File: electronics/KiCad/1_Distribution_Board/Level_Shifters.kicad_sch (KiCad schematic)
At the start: 26 parts, among them J25 Generic 2.54mm, J26 Generic 2.54mm, J27 Generic 2.54mm, J28 Generic 2.54mm, J29 Generic 2.54mm, J30 Generic 2.54mm, J31 Conn_01x04, J32 Conn_01x04, Q2 TBD, Q3 TBD

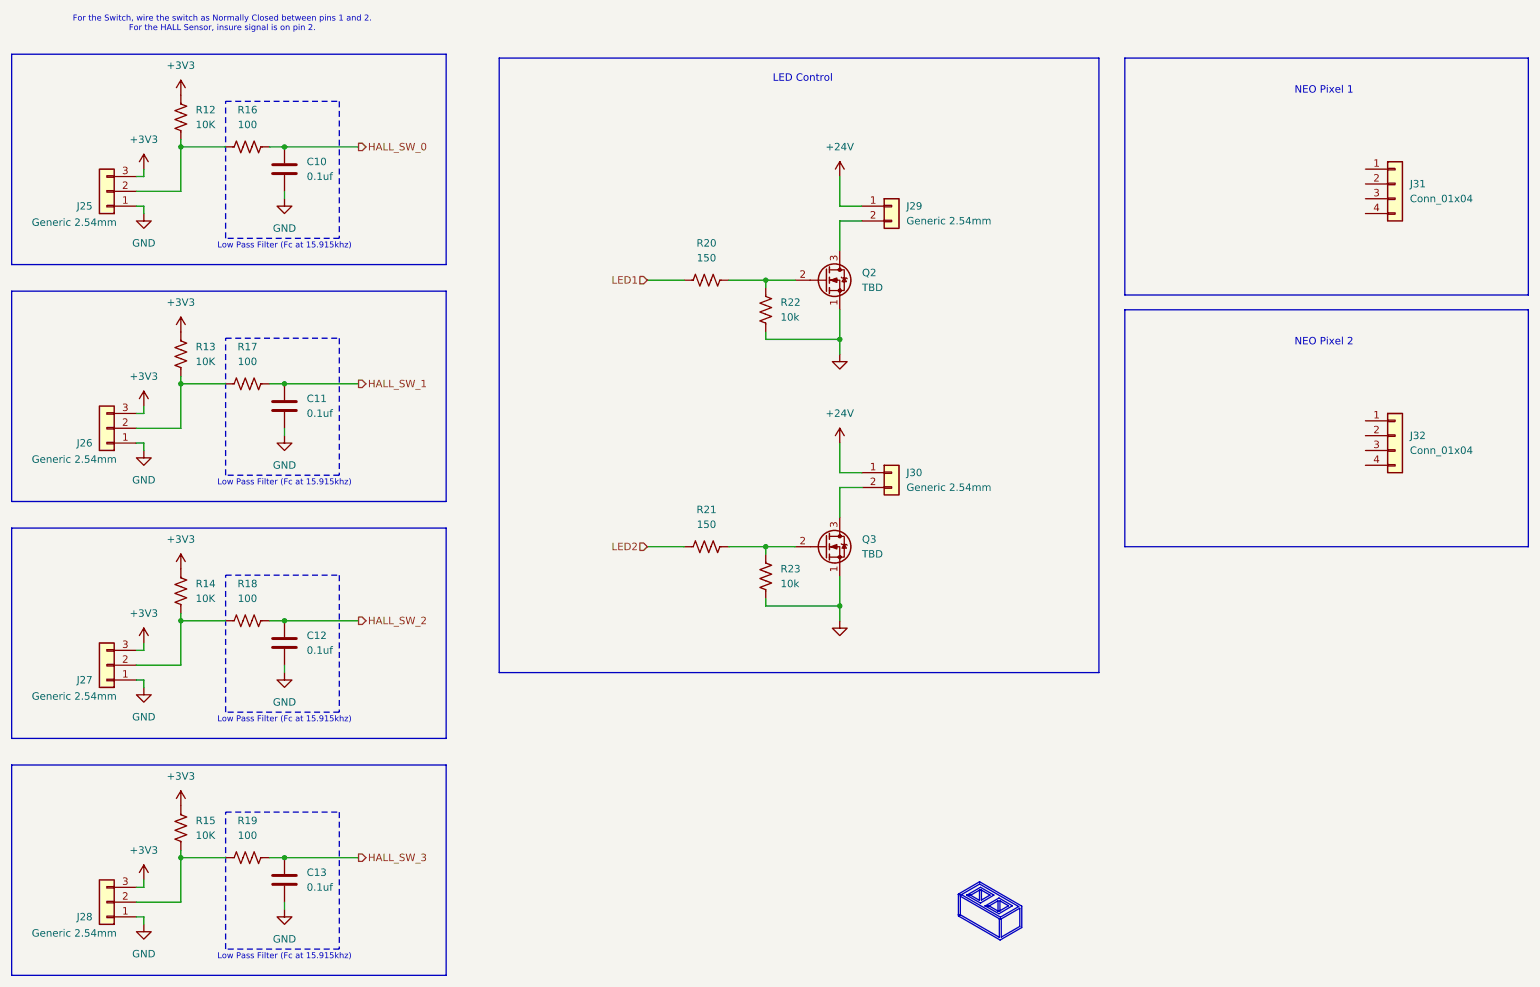
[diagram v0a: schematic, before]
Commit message: Additional Routing and placement
Updated power page on schematic to remove redundant connections. Removed test points on steppers since the steppers drivers chosen have test points on them. Updated placement and cleaned up silk. Started placing final power connections.
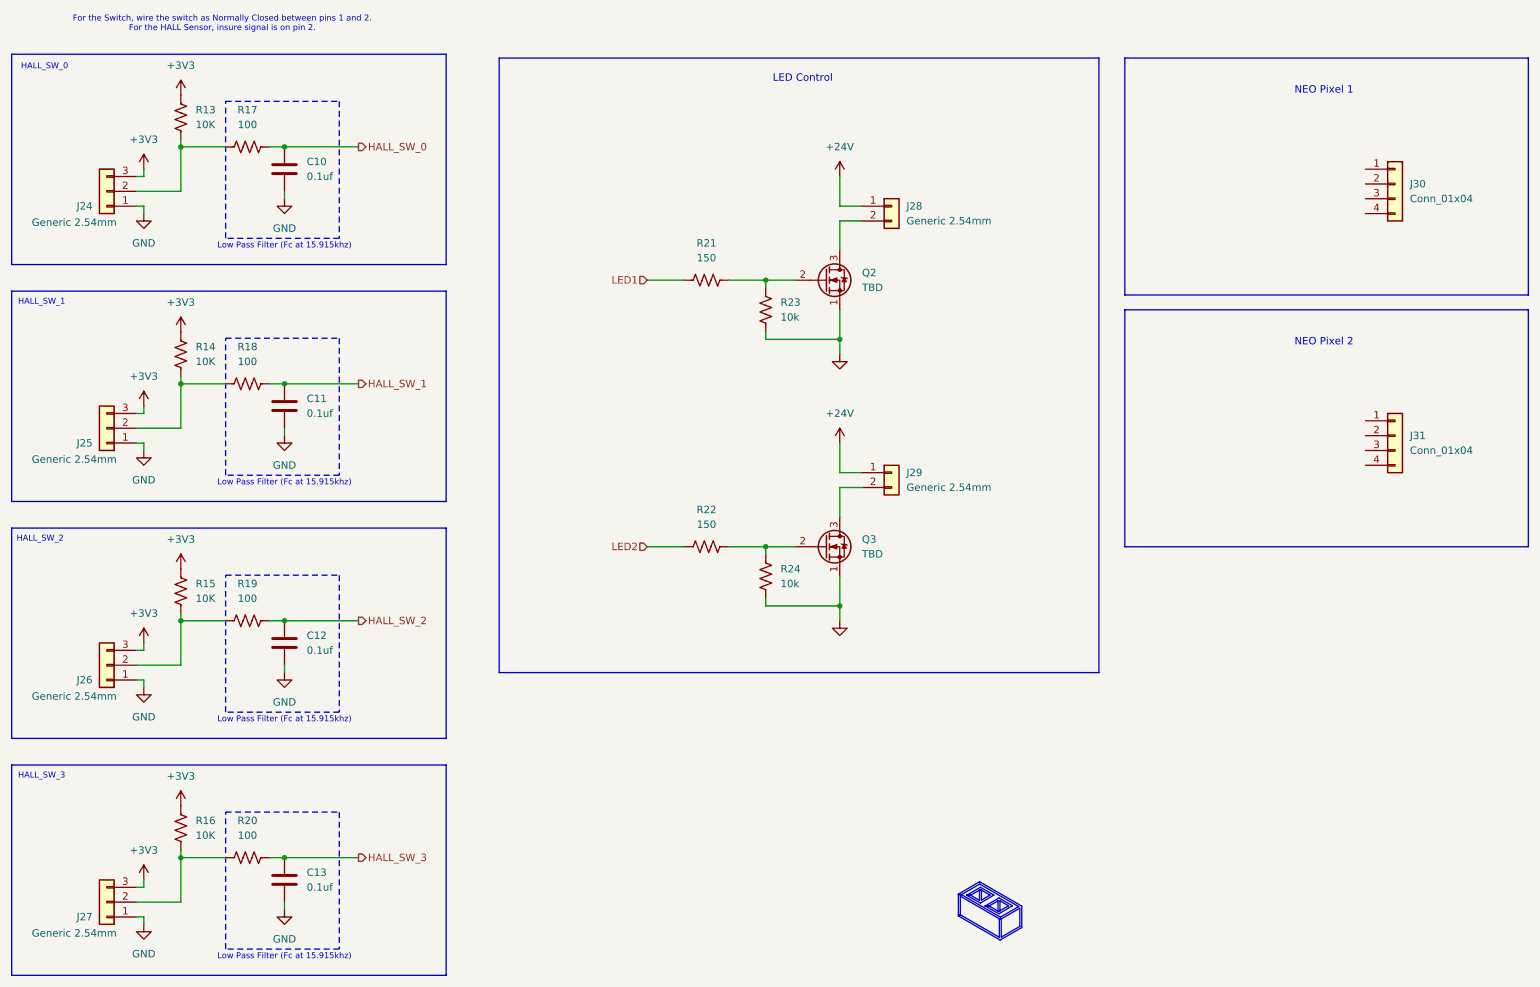
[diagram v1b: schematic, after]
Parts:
- renumbered J25 to J24, J26 to J25, J27 to J26, J28 to J27, J29 to J28, J30 to J29, J31 to J30, J32 to J31, R12 to R13, R13 to R14, R14 to R15, R15 to R16, R16 to R17, R17 to R18, R18 to R19, R19 to R20, R20 to R21, R21 to R22, R22 to R23, R23 to R24
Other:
- note added: "HALL_SW_0"
- note added: "HALL_SW_1"
- note added: "HALL_SW_2"
- note added: "HALL_SW_3"

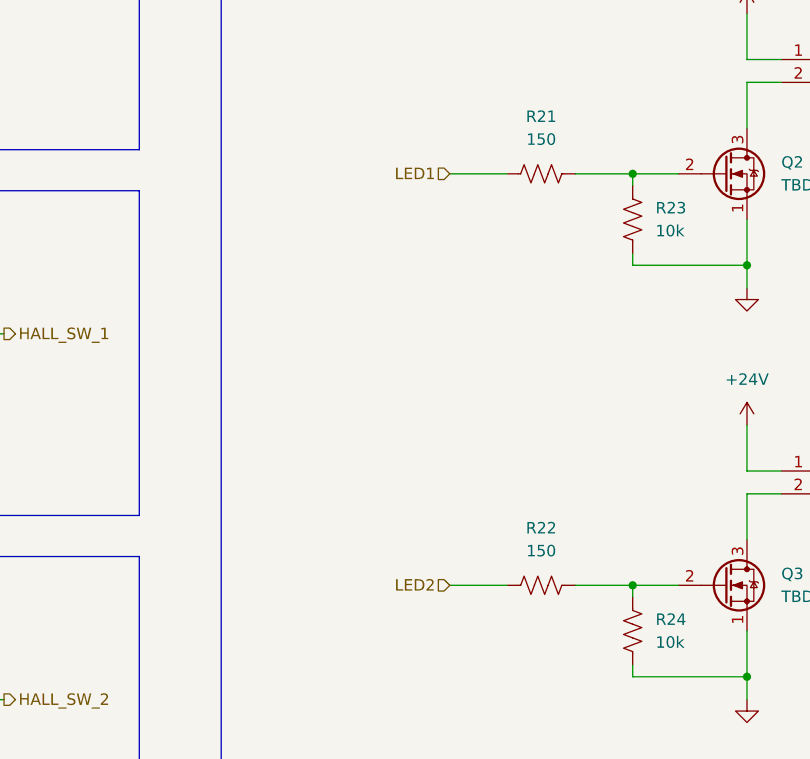
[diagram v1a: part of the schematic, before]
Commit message: Full Layout V0.1 Distributor
Full layout of distributor complete and ready for review. SCH updated but needs main page cleaned up.
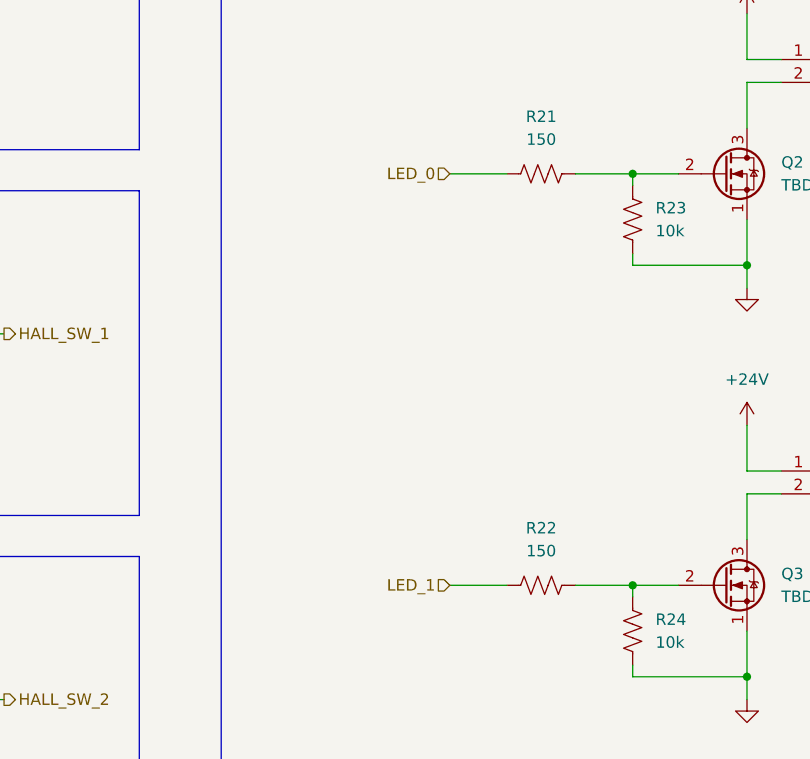
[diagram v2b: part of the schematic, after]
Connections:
- net LED1 renamed LED_0
- net LED2 renamed LED_1
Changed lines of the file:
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@@
 		)
 	)
-	(hierarchical_label "LED2"
+	(hierarchical_label "LED_1"
 		(shape input)
 		(at 127 110.49 180)
@@
 		)
 	)
-	(hierarchical_label "LED1"
+	(hierarchical_label "LED_0"
 		(shape input)
 		(at 127 64.77 180)

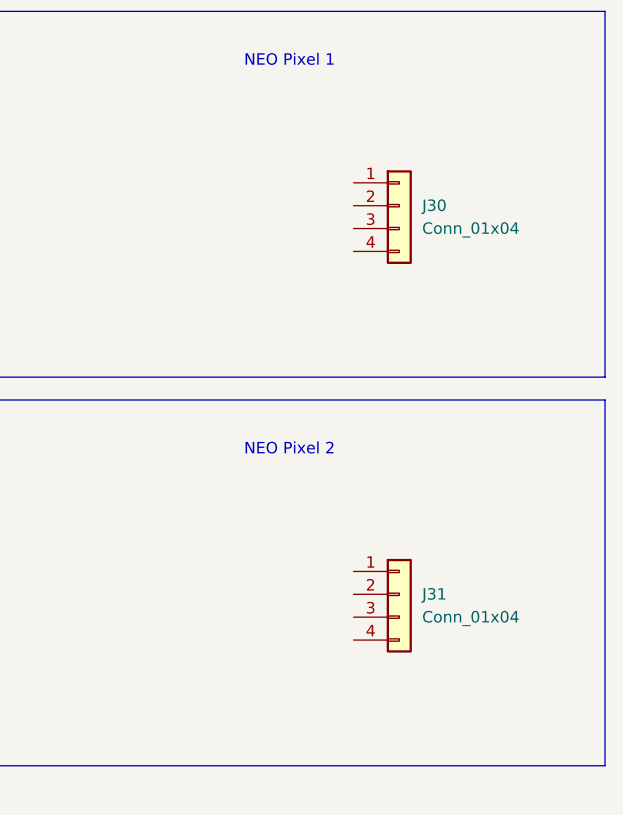
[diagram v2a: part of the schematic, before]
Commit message: SCH Cleanup for review
Cleaned up Processor page and cleaned up all other pages with notes for clarity
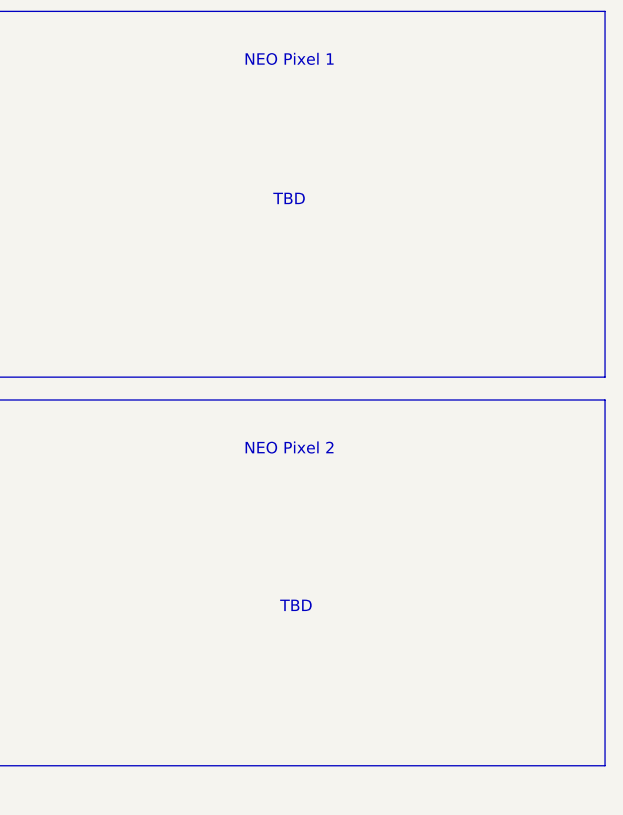
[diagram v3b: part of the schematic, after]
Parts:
- removed J30, J31: Conn_01x04, symbol Connector_Generic:Conn_01x04
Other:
- note added: "TBD"
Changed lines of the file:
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@@
 	(title_block
 		(title "Distribution Board")
-		(date "2026-01-25")
-		(rev "0.4")
+		(date "2026-02-05")
+		(rev "0.5")
 		(company "basically")
 	)
@@
 		)
 	)
+	(text "TBD"
+		(exclude_from_sim no)
+		(at 243.84 92.964 0)
+		(effects
+			(font
+				(size 1.27 1.27)
+			)
+		)
+	)
 	(text "HALL_SW_0"
 		(exclude_from_sim no)
@@
 		)
 	)
+	(text "TBD"
+		(exclude_from_sim no)
+		(at 243.078 47.752 0)
+		(effects
+			(font
+				(size 1.27 1.27)
+			)
+		)
+	)
 	(text "HALL_SW_2"
 		(exclude_from_sim no)
@@
 	)
 	(symbol
-		(lib_id "Connector_Generic:Conn_01x04")
-		(at 255.27 91.44 0)
-		(unit 1)
-		(exclude_from_sim no)
-		(in_bom yes)
-		(on_board yes)
-		(dnp no)
-		(fields_autoplaced yes)
-		(property "Reference" "J31"
-			(at 257.81 91.4399 0)
-			(effects
-				(font
-					(size 1.27 1.27)
-				)
-				(justify left)
-			)
-		)
-		(property "Value" "Conn_01x04"
-			(at 257.81 93.9799 0)
-			(effects
-				(font
-					(size 1.27 1.27)
-				)
-				(justify left)
-			)
-		)
-		(property "Footprint" ""
-			(at 255.27 91.44 0)
-			(effects
-				(font
-					(size 1.27 1.27)
-				)
-				(hide yes)
-			)
-		)
-		(property "Datasheet" "~"
-			(at 255.27 91.44 0)
-			(effects
-				(font
-					(size 1.27 1.27)
-				)
-				(hide yes)
-			)
-		)
-		(property "Description" "Generic connector, single row, 01x04, script generated (kicad-library-utils/schlib/autogen/connector/)"
-			(at 255.27 91.44 0)
-			(effects
-				(font
-					(size 1.27 1.27)
-				)
-				(hide yes)
-			)
-		)
-		(pin "2"
-		)
-		(pin "4"
-		)
-		(pin "3"
-		)
-		(pin "1"
-		)
-		(instances
-			(project "1_Distribution_Board"
-				(path "/d53c8c01-e754-4310-8a73-7d7c95e64cd3/aa124a9b-4ca6-4e8b-864b-f6c7e5891937"
-					(reference "J31")
-					(unit 1)
-				)
-			)
-		)
-	)
-	(symbol
 		(lib_id "Device:R_US")
 		(at 137.16 64.77 90)
@@
 					(unit 1)
 				)
-			)
-		)
-	)
-	(symbol
-		(lib_id "Connector_Generic:Conn_01x04")
-		(at 255.27 48.26 0)
-		(unit 1)
-		(exclude_from_sim no)
-		(in_bom yes)
-		(on_board yes)
-		(dnp no)
-		(fields_autoplaced yes)
-		(property "Reference" "J30"
-			(at 257.81 48.2599 0)
-			(effects
-				(font
-					(size 1.27 1.27)
-				)
-				(justify left)
-			)
-		)
-		(property "Value" "Conn_01x04"
-			(at 257.81 50.7999 0)
-			(effects
-				(font
-					(size 1.27 1.27)
-				)
-				(justify left)
-			)
-		)
-		(property "Footprint" ""
-			(at 255.27 48.26 0)
-			(effects
-				(font
-					(size 1.27 1.27)
-				)
-				(hide yes)
-			)
-		)
-		(property "Datasheet" "~"
-			(at 255.27 48.26 0)
-			(effects
-				(font
-					(size 1.27 1.27)
-				)
-				(hide yes)
-			)
-		)
-		(property "Description" "Generic connector, single row, 01x04, script generated (kicad-library-utils/schlib/autogen/connector/)"
-			(at 255.27 48.26 0)
-			(effects
-				(font
-					(size 1.27 1.27)
-				)
-				(hide yes)
-			)
-		)
-		(pin "2"
-		)
-		(pin "4"
-		)
-		(pin "3"
-		)
-		(pin "1"
-		)
-		(instances
-			(project "1_Distribution_Board"
-				(path "/d53c8c01-e754-4310-8a73-7d7c95e64cd3/aa124a9b-4ca6-4e8b-864b-f6c7e5891937"
-					(reference "J30")
-					(unit 1)
-				)

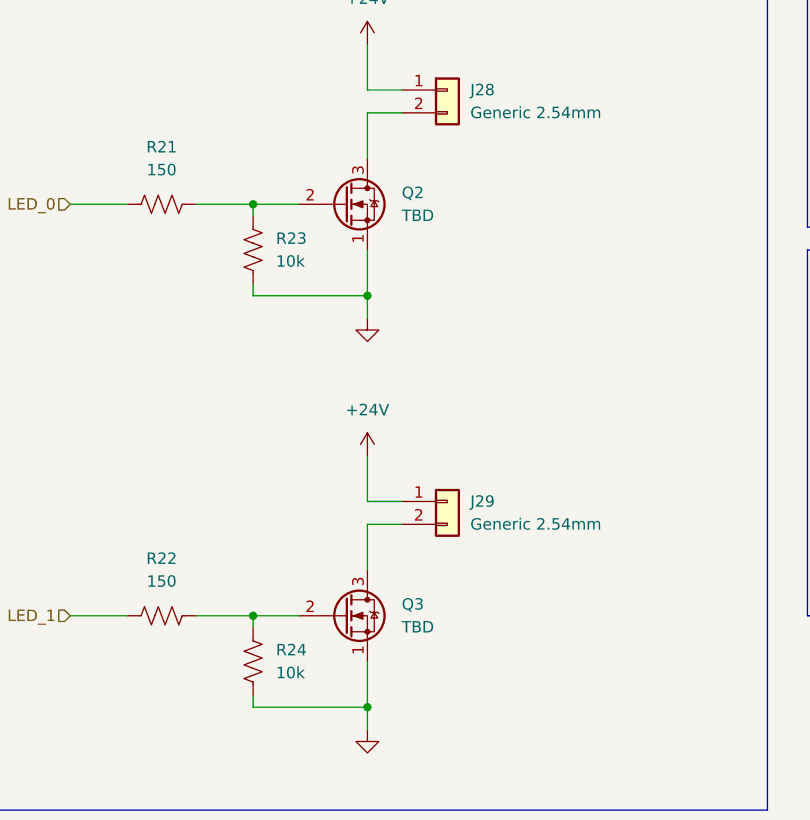
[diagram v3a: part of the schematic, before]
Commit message: Final Update for assembly order
Includes BOM and a minor update to LED FETs for pinout adjustment to match part choice.
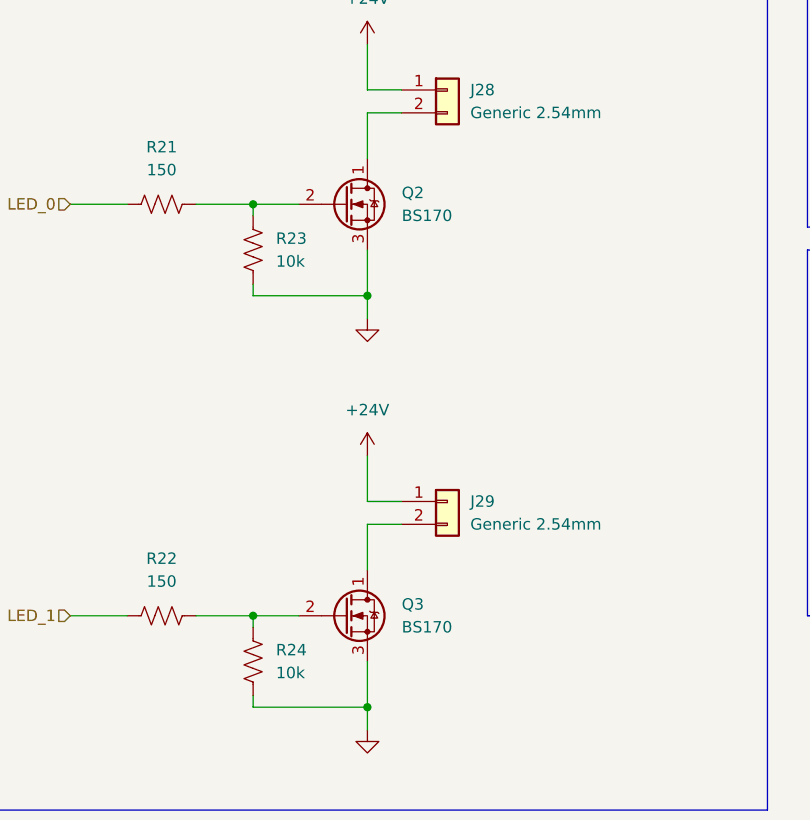
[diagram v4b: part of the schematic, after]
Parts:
- removed Q2, Q3: TBD, Package_TO_SOT_THT:TO-92_Inline, symbol Transistor_FET:2N7000
- added Q2, Q3: BS170, Package_TO_SOT_THT:TO-92_Inline, symbol Transistor_FET:BS170
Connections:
- net GND: now also Q2.3 (S), Q3.3 (S)
- net at R22.2, R24.1: now also Q3.2 (G)
- net at R21.2, R23.1: now also Q2.2 (G)
- net at J29.2 (Pin_2): now also Q3.1 (D)
- net at J28.2 (Pin_2): now also Q2.1 (D)
